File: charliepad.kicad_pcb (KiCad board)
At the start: 2 copper layers, 54 x 79.4 mm, 32 parts, among them J1 USB4105-GF-A, M2 MountingHole_2.2mm_M2_Pad_Via, SW1 SW_PUSH, SW10 SW_PUSH, SW11 SW_PUSH, SW12 SW_PUSH, SW2 SW_PUSH, SW3 SW_PUSH, SW4 SW_PUSH, SW5 SW_PUSH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

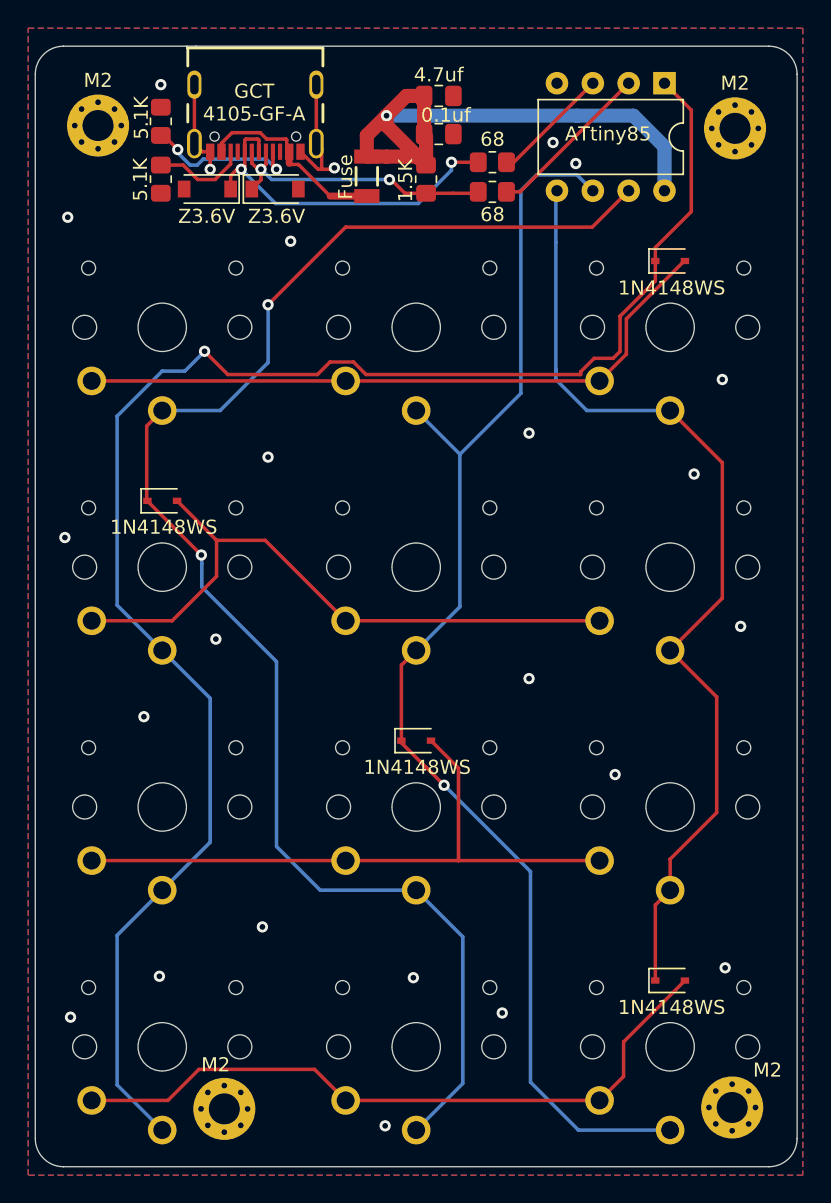
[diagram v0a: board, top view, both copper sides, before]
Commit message: Regularize track width Re-layout all the things, add logos, simple fw
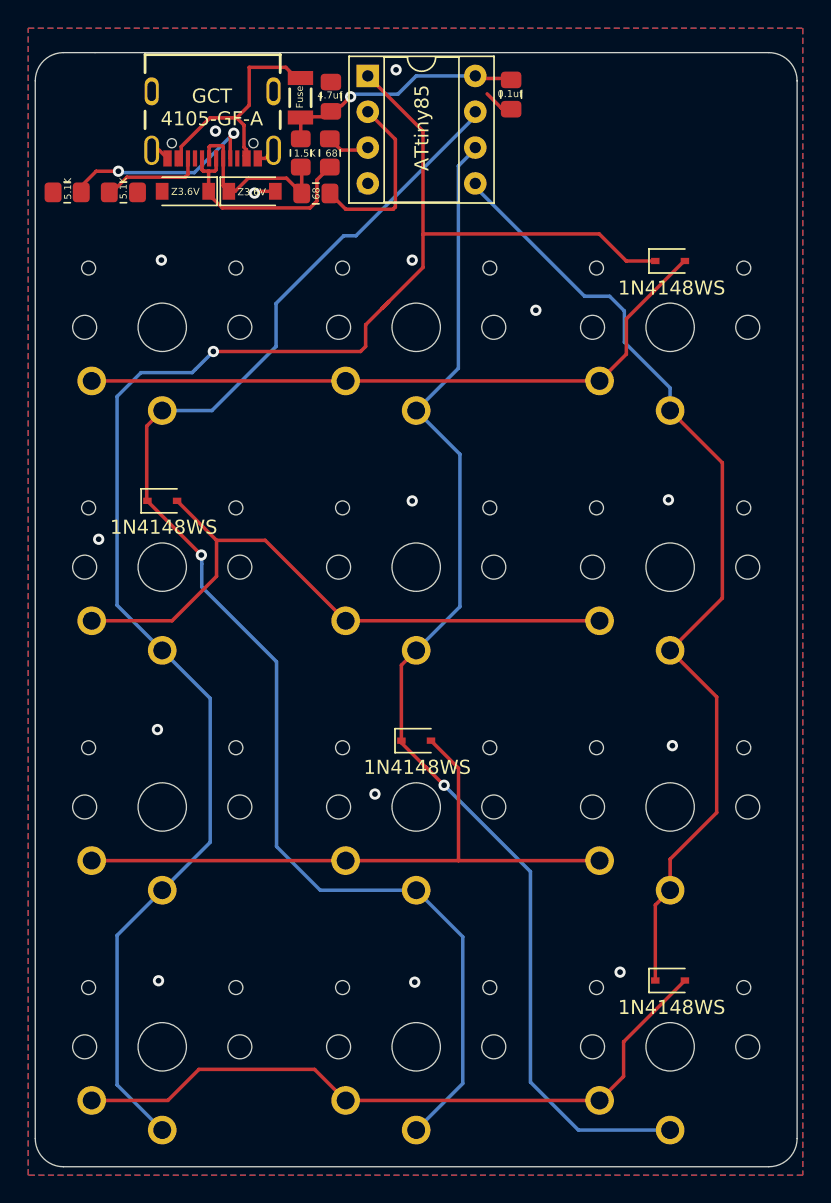
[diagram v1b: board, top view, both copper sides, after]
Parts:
- removed M2 (x4): MountingHole_2.2mm_M2_Pad_Via, MountingHole:MountingHole_2.2mm_M2_Pad_Via
- added G***: LOGO, footprints:alebrije, B.Cu at (79.3, 134.6)
- added G***: LOGO, footprints:charliepad, F.Cu at (95.5, 94.5)
- F1: value 1206L050YR -> Polyfuse 1206L050YR
- U1: footprint Package_DIP:DIP-8_W7.62mm -> Package_DIP:DIP-8_W7.62mm_Socket
- moved U1 21.0 mm to (75.9, 90.9), turned to 0 degrees
- moved R3 12.5 mm to (72.2, 99.2)
- moved R2 11.5 mm to (73.2, 96.3), turned to 270 degrees
- moved R1 9.07 mm to (71.1, 96.3)
- moved R4 8.33 mm to (54.6, 99.1), turned to 180 degrees
- moved C1 7.65 mm to (73.3, 92.4), turned to 90 degrees
- moved F1 7.29 mm to (71.1, 92.4)
- moved C2 5.84 mm to (86.0, 92.2), turned to 270 degrees
- moved J1 3.07 mm to (64.9, 92.0)
- moved R5 2.81 mm to (58.5, 99.1), turned to 180 degrees
- moved D2 1.64 mm to (67.7, 99.1)
- moved D1 1.57 mm to (62.9, 99.1)
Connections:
- F1 pad 1: VBUS -> +5V
- F1 pad 2: +5V -> VBUS
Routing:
- net +5V: track 44.9 -> 17.3 mm
- net D+: track 25.3 -> 15.4 mm, vias 2 -> 0
- net PB2: track 108.0 -> 98.8 mm, vias 2 -> 1
- net GND: track 15.9 -> 7.14 mm, vias 24 -> 15
- net D-: track 20.9 -> 13.1 mm, vias 2 -> 0
- net PB1: track 92.2 -> 85.9 mm
- net PB4: track 8.58 -> 2.95 mm
- net VBUS: track 13.5 -> 18.8 mm
- net Net-(J1-PadA5): track 11.1 -> 15.1 mm
- net PB3: track 11.8 -> 12.7 mm
- net PB5: track 119.1 -> 118.4 mm
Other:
- board size 54 x 79.4 mm -> 54 x 79 mm
